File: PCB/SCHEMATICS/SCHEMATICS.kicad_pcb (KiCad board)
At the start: 2 copper layers, 100 x 100 mm, 97 parts, among them IC1 CP2102-GMR, J1 Conn_01x24_Pin, J2 Conn_01x24_Pin, Q1 PMOS, U1 C7433, U2 AMS1117-3.3, U3 LTR-303ALS-01, U4 AMS1117-3.3, U5 LTR-303ALS-01, U6 C6482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

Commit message: Updating PCB
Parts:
- R40: value Value: Value: Value: 510k -> 510k
- moved MicroXNJ1 166.1 mm to (95.0, 83.8)
- moved R27 163.4 mm to (99.1, 84.8)
- moved R25 163.4 mm to (99.0, 83.3)
- moved R28 161.9 mm to (101.6, 84.8)
- moved R26 161.9 mm to (101.6, 83.3)
- moved IC1 154.0 mm to (108.7, 83.8)
- moved TP30 146.5 mm to (180.3, 44.7)
- moved R15 145.2 mm to (175.8, 54.4), turned to 90 degrees
- moved R8 141.4 mm to (183.4, 50.0), turned to -90 degrees
- moved R40 138.9 mm to (182.4, 52.3)
- moved D3 138.7 mm to (186.8, 61.5), turned to 180 degrees
- moved R10 137.9 mm to (180.8, 50.0), turned to 90 degrees
- moved D5 137.0 mm to (175.8, 51.0), turned to -90 degrees
- moved U1 134.7 mm to (184.4, 56.9), turned to 90 degrees
- moved R9 134.2 mm to (178.3, 50.3), turned to -90 degrees
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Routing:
- net GND: track 0.00 -> 90.0 mm
- net Net-(D5-K): track 0.00 -> 25.2 mm
- net Net-(D3-K): track 0.00 -> 17.6 mm
- net Net-(R12-Pad2): track 0.00 -> 12.5 mm
- net Net-(U1--): track 0.00 -> 8.64 mm
- net Net-(Q1-G): track 0.00 -> 6.29 mm
- net Net-(D3-A): track 0.00 -> 5.86 mm
- net /MICROCONTROLLER/PA0: track 0.00 -> 5.84 mm
- net /MICROCONTROLLER/PA1: track 0.00 -> 5.62 mm
- net /MICROCONTROLLER/PA2: track 0.00 -> 5.53 mm
- net Net-(D8-A): track 0.00 -> 5.05 mm
- net Net-(D7-A): track 0.00 -> 5.03 mm
- net Net-(D6-A): track 0.00 -> 5.02 mm
- net /POWER MODULE/Battery: track 0.00 -> 4.48 mm
- net Net-(Q1-D): track 0.00 -> 4.15 mm
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
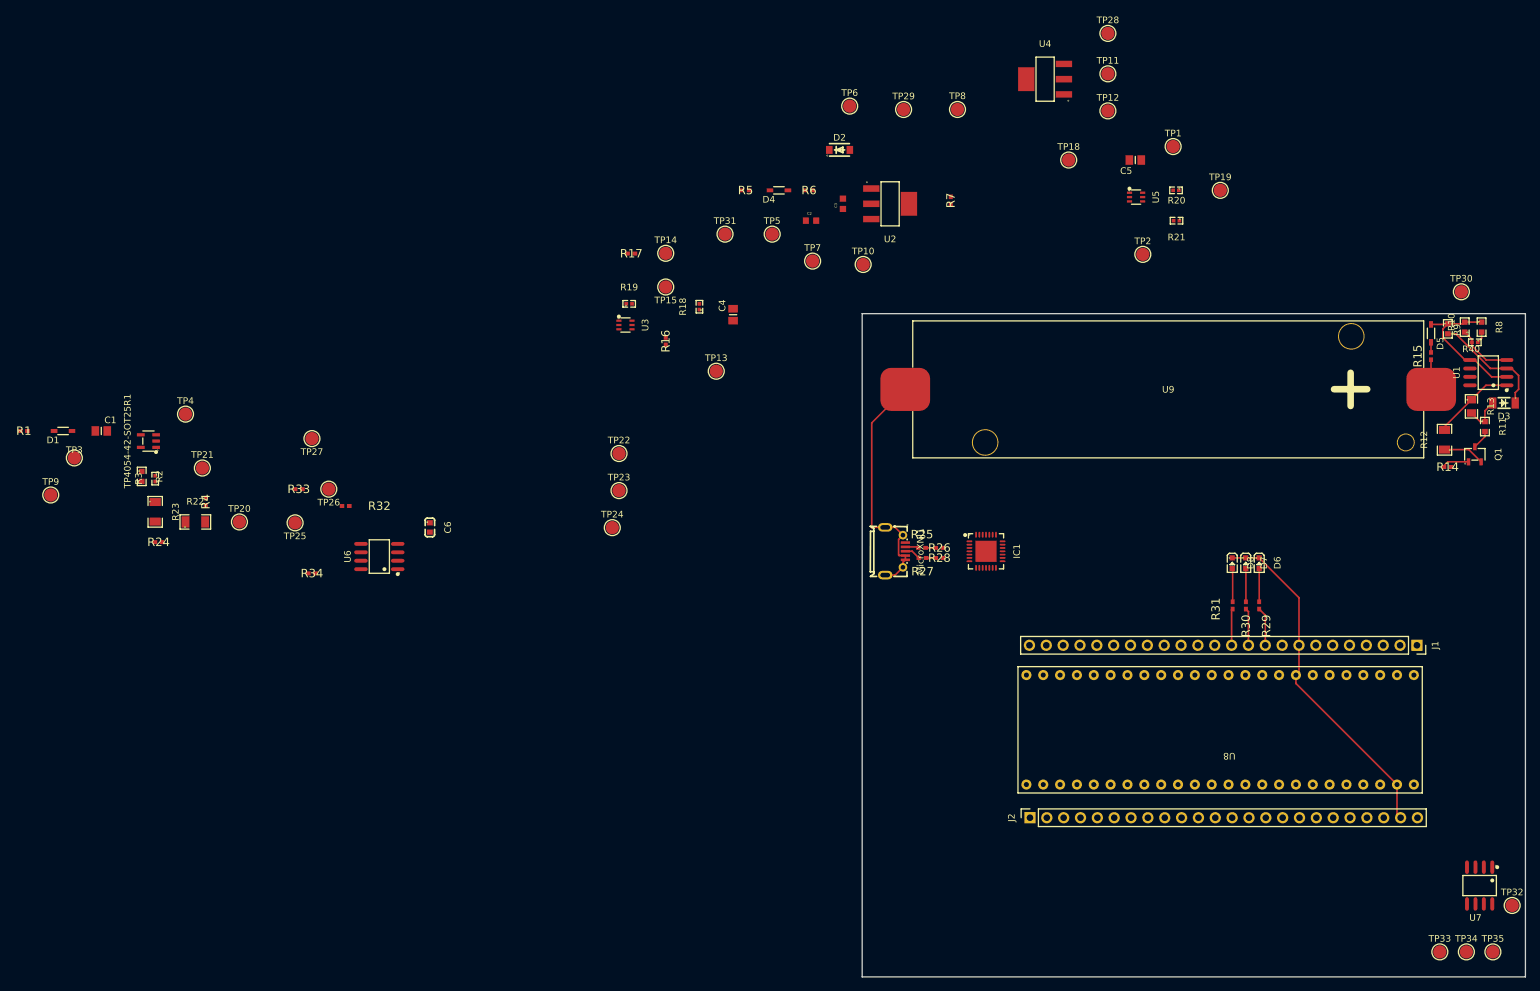
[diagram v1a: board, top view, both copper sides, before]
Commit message: updated traces
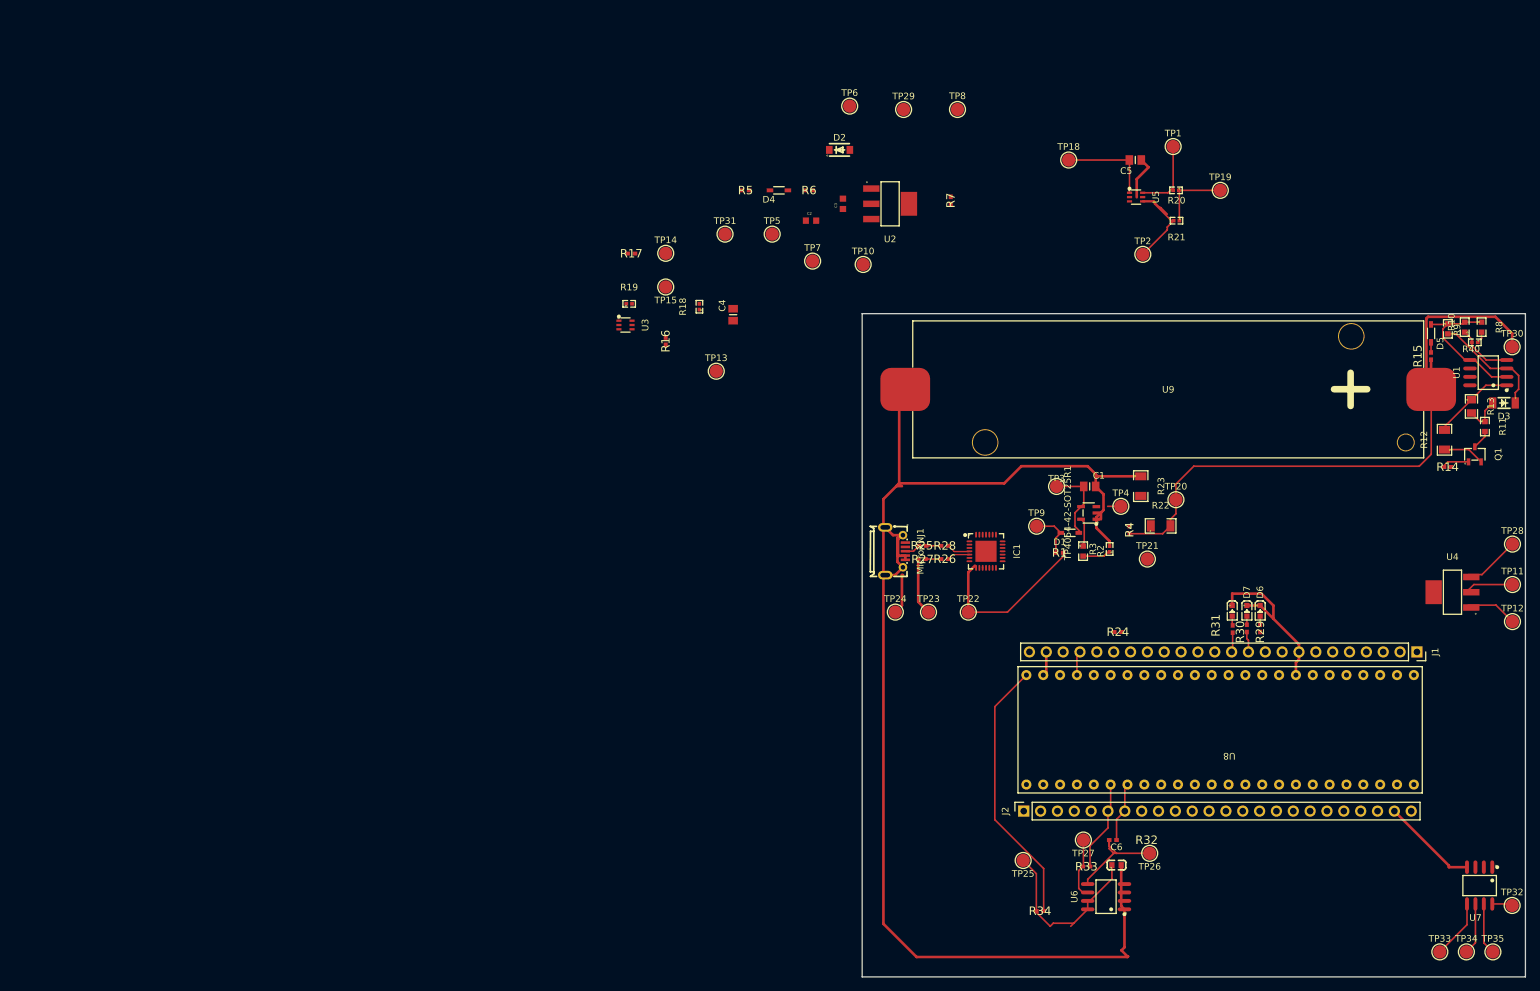
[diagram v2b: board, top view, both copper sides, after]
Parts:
- moved R1 157.2 mm to (119.8, 84.1), turned to 180 degrees
- moved D1 152.6 mm to (121.3, 81.1)
- moved C1 149.3 mm to (124.3, 74.1)
- moved TP9 148.7 mm to (116.3, 80.1)
- moved R23 148.6 mm to (132.0, 74.0)
- moved TP3 148.2 mm to (119.3, 74.1)
- moved R22 145.5 mm to (135.0, 80.0)
- moved R24 145.3 mm to (128.6, 96.0)
- moved R3 144.3 mm to (127.3, 83.5)
- moved TP21 143.1 mm to (133.0, 85.0)
- moved R2 142.4 mm to (123.3, 83.8)
- moved TP4054-42-SOT25R1 142.2 mm to (124.2, 78.1)
- moved TP4 141.7 mm to (129.0, 77.1)
- moved TP20 141.2 mm to (137.3, 76.1)
- moved R4 139.3 mm to (130.3, 80.6)
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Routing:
- net GND: track 90.0 -> 261.9 mm
- net /POWER MODULE/Battery: track 4.48 -> 95.0 mm
- net /MICROCONTROLLER/VSS: track 0.00 -> 40.6 mm
- net Net-(U6-VCC): track 0.00 -> 27.3 mm
- net /MICROCONTROLLER/5V: track 0.00 -> 25.8 mm
- net Net-(U5-SCL): track 0.00 -> 17.7 mm
- net Net-(U6-SDA): track 0.00 -> 16.4 mm
- net Net-(U5-VDD): track 0.00 -> 14.1 mm
- net /MICROCONTROLLER/PA9: track 0.00 -> 13.7 mm
- net Net-(D1-K): track 0.00 -> 12.0 mm
- net Net-(U5-SDA): track 0.00 -> 11.5 mm
- net Net-(R20-Pad1): track 0.00 -> 11.1 mm
- net Net-(U6-SCL): track 0.00 -> 9.19 mm
- net /MICROCONTROLLER/PA10: track 0.00 -> 9.05 mm
- net Net-(U7-SDA): track 0.00 -> 8.92 mm
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
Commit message: Updated pcb
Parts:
- removed U2, U4: AMS1117-3.3, footprint:SOT-223-4_L6.5-W3.5-P2.30-LS7.0-BR
- added REF1: AMS1117-3_3_C369933, footprint:SOT-223-4_L6.5-W3.5-P2.30-LS7.0-BR, F.Cu at (53.2, 84.0)
- added REF2: AMS1117-3_3_C369933, footprint:SOT-223-4_L6.5-W3.5-P2.30-LS7.0-BR, F.Cu at (178.4, 81.0)
- added TP16: TestPoint, TestPoint:TestPoint_Pad_D2.0mm, F.Cu at (104.3, 142.8)
- added TP17: TestPoint, TestPoint:TestPoint_Pad_D2.0mm, F.Cu at (102.3, 129.8)
- added TP36: TestPoint, TestPoint:TestPoint_Pad_D2.0mm, F.Cu at (113.3, 131.8)
- R40: value 510k -> Value: Value: Value: Value: Value: 510k
- moved TP1 123.0 mm to (99.4, 140.0), turned to 180 degrees
- moved TP31 122.5 mm to (187.0, 70.0)
- moved TP19 116.1 mm to (92.3, 133.4), turned to 180 degrees
- moved C5 116.1 mm to (105.1, 137.9), turned to 0 degrees
- moved TP18 113.3 mm to (115.1, 137.9), turned to 180 degrees
- moved R20 110.8 mm to (99.0, 133.4), turned to 0 degrees
- moved TP29 107.3 mm to (186.0, 76.0)
- moved U5 105.3 mm to (105.0, 132.4), turned to 90 degrees
- moved R21 102.3 mm to (98.9, 128.8), turned to 0 degrees
- moved TP2 93.4 mm to (106.3, 128.8), turned to 180 degrees
- moved U3 82.2 mm to (93.4, 122.0), turned to 180 degrees
- moved TP14 81.6 mm to (100.0, 110.2)
- moved TP15 81.6 mm to (100.0, 115.3)
- moved C4 81.6 mm to (110.2, 119.5)
- moved R17 81.6 mm to (96.0, 109.5), turned to 90 degrees
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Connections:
- C3 pad 1: GND -> Net-(D2-A)
- C5 pad 1: GND -> Net-(C5-Pad1)
- D2 pad 2: GND -> Net-(D2-A)
- R24 pad 2: /MICROCONTROLLER/PA3 -> /MICROCONTROLLER/PB9
- R7 pad 1: GND -> Net-(D2-A)
- TP25 pad : Net-(U6-VCC) -> (no net)
- TP29 pad 1: GND -> Net-(REF2-Input)
- TP6 pad 1: GND -> Net-(D2-A)
- TP8 pad 1: GND -> Net-(D2-A)
- U5 pad 3: GND -> Net-(U5-GND)
- U5 pad 5: GND -> Net-(U5-INT)
- U8 pad 38: /MICROCONTROLLER/PAQ15 -> /MICROCONTROLLER/PA15
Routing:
- net /MICROCONTROLLER/PB9: track 0.00 -> 87.6 mm
- net GND: track 261.9 -> 342.8 mm
- net /MICROCONTROLLER/VSS: track 40.6 -> 117.8 mm
- net /POWER MODULE/Battery: track 95.0 -> 65.4 mm
- net Net-(D2-K): track 0.00 -> 27.4 mm
- net Net-(R22-Pad1): track 0.00 -> 21.5 mm
- net Net-(D2-A): track 0.00 -> 18.8 mm
- net Net-(U3-SCL): track 0.00 -> 14.2 mm
- net /MICROCONTROLLER/PA0: track 0.00 -> 9.68 mm
- net /POWER MODULE/UVLO Output: track 0.43 -> 9.14 mm
- net /MICROCONTROLLER/PA10: track 9.05 -> 16.8 mm
- net Net-(U5-GND): track 0.00 -> 7.34 mm
- net Net-(U5-SCL): track 17.7 -> 10.5 mm
- net /MICROCONTROLLER/PA2: track 2.97 -> 9.97 mm
- net /MICROCONTROLLER/PA1: track 3.10 -> 9.90 mm
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
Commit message: Updating PCB
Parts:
- moved TP5 65.1 mm to (94.0, 108.2)
- moved R5 62.5 mm to (93.2, 103.8)
- moved TP7 60.3 mm to (102.0, 111.8)
- moved D2 60.1 mm to (106.7, 99.8)
- moved D4 60.1 mm to (97.8, 103.8)
- moved REF1 60.1 mm to (108.3, 107.8)
- moved C2 60.1 mm to (102.2, 106.0)
- moved R6 60.1 mm to (99.2, 107.3)
- moved TP10 60.1 mm to (99.2, 98.8)
- moved TP6 60.1 mm to (109.2, 92.8)
- moved C3 58.1 mm to (115.0, 99.1)
- moved TP8 45.9 mm to (117.0, 92.8)
- moved R7 44.7 mm to (115.5, 107.8)
- moved TP24 23.5 mm to (104.5, 76.8)
- moved MicroXNJ1 21.3 mm to (96.4, 81.2), turned to -90 degrees
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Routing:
- net GND: track 342.8 -> 88.3 mm, vias 0 -> 10
- net /POWER MODULE/UVLO Output: track 9.14 -> 190.2 mm
- net /MICROCONTROLLER/PA12: track 4.17 -> 124.6 mm
- net /MICROCONTROLLER/PA11: track 4.17 -> 121.0 mm
- net /MICROCONTROLLER/5V: track 25.8 -> 103.7 mm
- net /MICROCONTROLLER/VSS: track 117.8 -> 185.3 mm, vias 0 -> 3
- net /MICROCONTROLLER/PB10: track 3.91 -> 57.6 mm, vias 0 -> 1
- net /MICROCONTROLLER/PB11: track 3.68 -> 47.6 mm, vias 0 -> 1
- net /POWER MODULE/Battery: track 65.4 -> 95.3 mm
- net Net-(MicroXNJ1-D-): track 8.64 -> 28.0 mm
- net Net-(D2-A): track 18.8 -> 32.7 mm
- net Net-(U3-SDA): track 6.13 -> 19.5 mm
- net Net-(MicroXNJ1-D+): track 2.58 -> 15.1 mm
- net (no net): track 4.78 -> 0.00 mm
- net Net-(U3-SCL): track 14.2 -> 16.5 mm
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- added copper zone on B.Cu, net GND

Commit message: Made changes
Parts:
- R40: value Value: Value: Value: Value: Value: 510k -> Value: Value: Value: Value: Value: Value: 510k
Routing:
- net /MICROCONTROLLER/PB10: track 57.6 -> 187.0 mm, vias 1 -> 2
- net /POWER MODULE/UVLO Output: track 190.2 -> 121.9 mm, vias 0 -> 2
- net /MICROCONTROLLER/VSS: track 185.3 -> 249.7 mm, vias 3 -> 4
- net (no net): track 0.00 -> 63.2 mm
- net /MICROCONTROLLER/5V: track 103.7 -> 66.6 mm, vias 0 -> 4
- net /POWER MODULE/Battery: track 95.3 -> 77.9 mm, vias 0 -> 2
- net Net-(U3-SCL): track 16.5 -> 31.9 mm, vias 0 -> 1
- net Net-(#FLG06-pwr): track 25.2 -> 37.2 mm, vias 0 -> 2
- net GND: track 88.3 -> 77.2 mm, vias 10 -> 14

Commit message: Updating PCB
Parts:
- R40: value Value: Value: Value: Value: Value: Value: 510k -> 510k
- moved TP25 0.60 mm to (139.0, 132.8)
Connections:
- TP25 pad : (no net) -> Net-(U6-VCC)
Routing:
- net (no net): track 63.2 -> 0.00 mm
- net /MICROCONTROLLER/VSS: track 249.7 -> 269.5 mm
- net Net-(U3-SCL): track 31.9 -> 29.5 mm, vias 1 -> 2
- net Net-(U6-VCC): track 27.3 -> 26.1 mm
- net /MICROCONTROLLER/PB10: vias 2 -> 1

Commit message: Updating PCB
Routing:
- net GND: track 77.5 -> 74.1 mm
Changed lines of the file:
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@@
     (property "ki_keywords" "r resistor")
     (attr smd)
-    (fp_text reference "R33" (at 0 0) (layer "F.SilkS")
+    (fp_text reference "R33" (at 0 -1.568504) (layer "F.SilkS")
         (effects (font (size 1.27 1.27) (thickness 0.254)))
     )
@@
         (effects (font (size 1.27 1.27) (thickness 0.254)))
     )
-    (fp_text user "${REFERENCE}" (at 0 0) (layer "F.Fab")
+    (fp_text user "${REFERENCE}" (at 0 -1.568504) (layer "F.Fab")
         (effects (font (size 1.27 1.27) (thickness 0.254)))
     )
@@
         (effects (font (size 1.27 1.27) (thickness 0.254)))
     )
-    (fp_text user "${REFERENCE}" (at -0.45 -2 90) (layer "F.Fab")
+    (fp_text user "${REFERENCE}" (at 0.27 -3 90) (layer "F.Fab")
         (effects (font (size 1.27 1.27) (thickness 0.254)))
     )
@@
         (effects (font (size 1 1) (thickness 0.15)))
     )
-    (fp_text value "D_Schottky" (at -0.174 2.032) (layer "F.Fab")
+    (fp_text value "D_Schottky" (at -0.9302 1.799975) (layer "F.Fab")
         (effects (font (size 1 1) (thickness 0.15)))
     )
@@
     (property "ki_keywords" "cap capacitor")
     (attr smd)
-    (fp_text reference "C3" (at -0.24 -1.07 90) (layer "F.SilkS")
-        (effects (font (size 0.393701 0.393701) (thickness 0.15)))
+    (fp_text reference "C3" (at -0.24 -1.530289 90) (layer "F.SilkS")
+        (effects (font (size 0.8 0.393701) (thickness 0.098425)))
     )
     (fp_text value "10uF" (at 1.51 1.07 90) (layer "F.Fab")
@@
         (effects (font (size 1 1) (thickness 0.15)))
     )
-    (fp_text value "TestPoint" (at 2 -0.2 -90) (layer "F.Fab")
+    (fp_text value "TestPoint" (at 2 -0.2 -90) (layer "F.Fab") hide
         (effects (font (size 1 1) (thickness 0.15)))
     )
@@
     (attr through_hole)
     (fp_text reference "TP4054-42-SOT25R1" (at 3.753538 -2.63017 90) (layer "F.SilkS")
-        (effects (font (size 0.5 0.5) (thickness 0.05)))
+        (effects (font (size 0.8 0.5) (thickness 0.08)))
     )
     (fp_text value "~" (at 0 3.15367 90) (layer "F.Fab")
@@
         (effects (font (size 1 1) (thickness 0.15)))
     )
-    (fp_text value "1N4001" (at 0 2.933147) (layer "F.Fab")
+    (fp_text value "1N4001" (at 0.030289 1.950025) (layer "F.Fab")
         (effects (font (size 1 1) (thickness 0.15)))
     )
@@
     (property "ki_keywords" "r resistor")
     (attr smd)
-    (fp_text reference "R32" (at 5.08 0) (layer "F.SilkS")
+    (fp_text reference "R32" (at 3.528916 -0.431496) (layer "F.SilkS")
         (effects (font (size 1.27 1.27) (thickness 0.254)))
     )
@@
         (effects (font (size 1 1) (thickness 0.15)))
     )
-    (fp_text value "TestPoint" (at 0 2.05) (layer "F.Fab")
+    (fp_text value "TestPoint" (at 0 2.05) (layer "F.Fab") hide
         (effects (font (size 1 1) (thickness 0.15)))
     )
@@
         (effects (font (size 1 1) (thickness 0.15)))
     )
-    (fp_text value "TestPoint" (at 0 2.05) (layer "F.Fab")
+    (fp_text value "TestPoint" (at 0 2.05) (layer "F.Fab") hide
         (effects (font (size 1 1) (thickness 0.15)))
     )
@@
     (property "ki_keywords" "capacitor cap")
     (attr through_hole)
-    (fp_text reference "C6" (at -0.007722 -2.715443) (layer "F.SilkS")
+    (fp_text reference "C6" (at 2.171084 -2.848529) (layer "F.SilkS")
         (effects (font (size 1 1) (thickness 0.15)))
     )
-    (fp_text value "3.3nF" (at -0.007722 2.710033) (layer "F.Fab")
+    (fp_text value "3.3nF" (at 0.421084 -1.598529) (layer "F.Fab")
         (effects (font (size 1 1) (thickness 0.15)))
     )
@@
     (property "ki_keywords" "r resistor")
     (attr smd)
-    (fp_text reference "R16" (at 0 0) (layer "F.SilkS")
+    (fp_text reference "R16" (at -0.7 1.72) (layer "F.SilkS")
         (effects (font (size 1.27 1.27) (thickness 0.254)))
     )
@@
         (effects (font (size 1.27 1.27) (thickness 0.254)))
     )
-    (fp_text user "${REFERENCE}" (at 0 0) (layer "F.Fab")
+    (fp_text user "${REFERENCE}" (at -0.7 1.72) (layer "F.Fab")
         (effects (font (size 1.27 1.27) (thickness 0.254)))
     )
@@
         (effects (font (size 1 1) (thickness 0.15)))
     )
-    (fp_text value "TestPoint" (at 2 1.28 90) (layer "F.Fab")
+    (fp_text value "TestPoint" (at 2 1.28 90) (layer "F.Fab") hide
         (effects (font (size 1 1) (thickness 0.15)))
     )
@@
     (property "ki_keywords" "C369933")
     (attr through_hole)
-    (fp_text reference "REF1" (at 0 -5.326213) (layer "F.SilkS")
-        (effects (font (size 1 1) (thickness 0.15)))
-    )
-    (fp_text value "AMS1117-3_3_C369933" (at 0 5.326213) (layer "F.Fab")
+    (fp_text reference "REF1" (at 0 -5.326213) (layer "F.SilkS") hide
         (effects (font (size 1 1) (thickness 0.15)))
     )
-    (fp_text user "REF**" (at 0 7.326213) (layer "F.Fab")
-        (effects (font (size 1 1) (thickness 0.15)))
+    (fp_text value "AMS1117-3_3_C369933" (at -2.9151 4.299975) (layer "F.Fab")
+        (effects (font (size 0.5 0.5) (thickness 0.125)))
     )
     (fp_line (start -1.3714 -3.326213) (end 1.3714 -3.326213)
@@
     (property "ki_keywords" "test point tp")
     (attr exclude_from_pos_files)
-    (fp_text reference "TP7" (at 0.25 4) (layer "F.SilkS")
+    (fp_text reference "TP7" (at 2.5 1.75) (layer "F.SilkS")
         (effects (font (size 1 1) (thickness 0.15)))
     )
@@
     (property "ki_keywords" "cap capacitor")
     (attr smd)
-    (fp_text reference "C2" (at -0.24 -1.07 90) (layer "F.SilkS")
-        (effects (font (size 0.393701 0.393701) (thickness 0.15)))
+    (fp_text reference "C2" (at -1.024975 -1.3302 90) (layer "F.SilkS")
+        (effects (font (size 0.8 0.393701) (thickness 0.098425) bold))
     )
-    (fp_text value "10uF" (at 1.51 1.07 90) (layer "F.Fab")
-        (effects (font (size 0.393701 0.393701) (thickness 0.15)))
+    (fp_text value "10uF" (at 0.475025 -1.3302 90) (layer "F.Fab")
+        (effects (font (size 0.8 0.393701) (thickness 0.098425)))
     )
     (fp_line (start -1.485 -0.735) (end 1.485 -0.735)
@@
         (effects (font (size 1 1) (thickness 0.15)))
     )
-    (fp_text value "TestPoint" (at 0 2.05) (layer "F.Fab")
+    (fp_text value "TestPoint" (at 0 2.05) (layer "F.Fab") hide
         (effects (font (size 1 1) (thickness 0.15)))
     )
@@
     (property "ki_keywords" "r resistor")
     (attr through_hole)
-    (fp_text reference "R19" (at -2.487183 -1.82 90) (layer "F.SilkS")
+    (fp_text reference "R19" (at -2.067183 0.04 90) (layer "F.SilkS")
         (effects (font (size 1 1) (thickness 0.15)))
     )
-    (fp_text value "1k" (at -1.487183 -1.82 90) (layer "F.Fab")
+    (fp_text value "1k" (at 2.682817 0.29 90) (layer "F.Fab")
         (effects (font (size 1 1) (thickness 0.15)))
     )
@@
         (effects (font (size 1 1) (thickness 0.15)))
     )
-    (fp_text value "TestPoint" (at 0 2.05) (layer "F.Fab")
+    (fp_text value "TestPoint" (at 0 2.05) (layer "F.Fab") hide
         (effects (font (size 1 1) (thickness 0.15)))
     )
@@
         (effects (font (size 1 1) (thickness 0.15)))
     )
-    (fp_text value "1uF" (at -0.126008 1.723992) (layer "F.Fab")
+    (fp_text value "1uF" (at -0.126008 1.973992) (layer "F.Fab")
         (effects (font (size 1 1) (thickness 0.15)))
     )
@@
         (effects (font (size 1 1) (thickness 0.15)))
     )
-    (fp_text value "C6482" (at 5.08 0 180) (layer "F.Fab")
+    (fp_text value "C6482" (at -3.891496 0 180) (layer "F.Fab")
         (effects (font (size 1 1) (thickness 0.15)))
     )
@@
   (segment (start 94.007491 131.1945) (end 94.007491 131.007491) (width 0.5) (layer "B.Cu") (net 5))
   (segment (start 154.568175 134.568175) (end 154.568175 134.359994) (width 0.5) (layer "B.Cu") (net 5))
-  (segment (start 95 64) (end 96 65) (width 0.5) (layer "B.Cu") (net 5))
-  (segment (start 96 65) (end 98 65) (width 0.5) (layer "B.Cu") (net 5))
   (segment (start 108.85 125.47) (end 109.41 126.03) (width 0.5) (layer "F.Cu") (net 6))
   (segment (start 92.517171 124.569998) (end 97.087169 120) (width 0.5) (layer "F.Cu") (net 6))
